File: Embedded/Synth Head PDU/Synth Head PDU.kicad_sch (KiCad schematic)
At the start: 0 parts

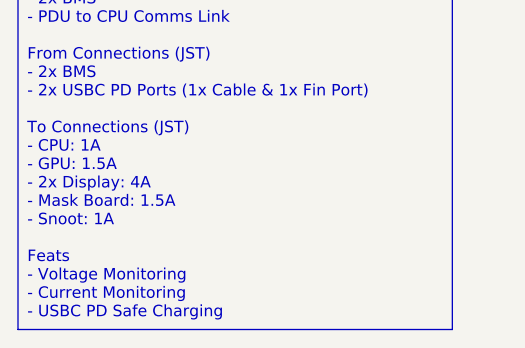
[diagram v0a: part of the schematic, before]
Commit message: KiCAD Added the schematics to drive some sensors
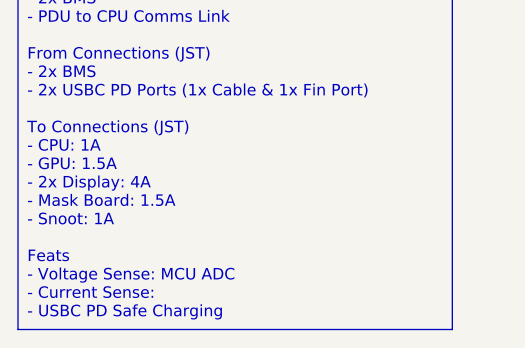
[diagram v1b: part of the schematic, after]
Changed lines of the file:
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@@
 	(generator_version "8.0")
 	(paper "A4")
-	(text_box "FFC\n- 2x BMS\n- PDU to CPU Comms Link\n\nFrom Connections (JST)\n- 2x BMS\n- 2x USBC PD Ports (1x Cable & 1x Fin Port)\n\nTo Connections (JST)\n- CPU: 1A\n- GPU: 1.5A\n- 2x Display: 4A\n- Mask Board: 1.5A\n- Snoot: 1A\n\nFeats\n- Voltage Monitoring\n- Current Monitoring\n- USBC PD Safe Charging"
+	(text_box "FFC\n- 2x BMS\n- PDU to CPU Comms Link\n\nFrom Connections (JST)\n- 2x BMS\n- 2x USBC PD Ports (1x Cable & 1x Fin Port)\n\nTo Connections (JST)\n- CPU: 1A\n- GPU: 1.5A\n- 2x Display: 4A\n- Mask Board: 1.5A\n- Snoot: 1A\n\nFeats\n- Voltage Sense: MCU ADC\n- Current Sense: \n- USBC PD Safe Charging"
 		(exclude_from_sim no)
 		(at 25.4 25.4 0)

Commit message: PDU Schematic Basically Completed
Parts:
- added D1: SL54A, Diode_SMD:D_SMA-SMB_Universal_Handsoldering, symbol Device:D
- added F1: Polyfuse, symbol Device:Polyfuse
- added J1: 10171746-00021LF, USBC_10171746_00021LF:AMPHENOL_10171746-00021LF, symbol USBC_10171746_00021LF:10171746-00021LF
- added J2, J3: JST [P], symbol Connector:Conn_01x12_Socket
- added J4: JST [USB], symbol Connector:Conn_01x06_Socket
- added J5: JST [C], symbol Connector:Conn_01x04_Socket
- added J6: JST [B], symbol Connector:Conn_01x04_Socket
- added J7: JST [G], symbol Connector:Conn_01x08_Socket
- added R1, R2: 5.1K, Resistor_SMD:R_0603_1608Metric, symbol Device:R
- added R3, R4: 4K, symbol Device:R
- added U1: FFC [K], FFC_Connector:FFC Aliexpress 0.5mm 6P, symbol FCC_Connector:FFC_6P
- added U2: TMCS1108A2BQDR, Package_SO:SOIC-8_3.9x4.9mm_P1.27mm, symbol TMCS1108:TMCS1108
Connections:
- new net: J1.A5 (CC1), R2.1
- new net: J1.B5 (CC2), R1.1
- new net: D1.1 (K), F1.1
- new net +3V3: U2.8 (VS)
- new net +5V: J5.2 (Pin_2), J5.3 (Pin_3), J6.2 (Pin_2), J6.3 (Pin_3), J7.3 (Pin_3), J7.4 (Pin_4), J7.5 (Pin_5), J7.6 (Pin_6)
- new net Analog Current: U1.5, U2.7 (Vout)
- new net Analog Voltage: R3.2, R4.1, U1.2
- new net GND: J1.A1_B12 (GND_A), J1.B1_A12 (GND_B), J1.SH1 (SHIELD), J1.SH2 (SHIELD__1), J1.SH3 (SHIELD__2), J1.SH4 (SHIELD__3), J2.1 (Pin_1), J2.10 (Pin_10), J2.11 (Pin_11), J2.12 (Pin_12), J2.2 (Pin_2), J2.3 (Pin_3), J3.1 (Pin_1), J3.10 (Pin_10), J3.11 (Pin_11), J3.12 (Pin_12), J3.2 (Pin_2), J3.3 (Pin_3), J4.1 (Pin_1), J4.6 (Pin_6), J5.1 (Pin_1), J5.4 (Pin_4), J6.1 (Pin_1), J6.4 (Pin_4), J7.1 (Pin_1), J7.2 (Pin_2), J7.7 (Pin_7), J7.8 (Pin_8), R1.2, R2.2, R4.2, U1.1, U1.6, U2.5 (GND)
- new net PWR: U2.3 (Output), U2.4 (Output)
- new net Raw PWR: F1.2, J2.4 (Pin_4), J2.5 (Pin_5), J2.6 (Pin_6), J2.7 (Pin_7), J2.8 (Pin_8), J2.9 (Pin_9), J3.4 (Pin_4), J3.5 (Pin_5), J3.6 (Pin_6), J3.7 (Pin_7), J3.8 (Pin_8), J3.9 (Pin_9), R3.1, U2.1 (Input), U2.2 (Input)
- new net USB +: J1.A6 (DP1), J1.B6 (DP2), J4.3 (Pin_3), U1.3
- new net USB -: J1.A7 (DN1), J1.B7 (DN2), J4.4 (Pin_4), U1.4
- new net USB PWR: D1.2 (A), J1.A4_B9 (VBUS_A), J1.B4_A9 (VBUS_B), J4.2 (Pin_2), J4.5 (Pin_5)
- no-connect marks 0 -> 2
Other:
- added sheet 3V3 Regulator (3V3 Reg.kicad_sch)

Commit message: PDU Nearly Complete
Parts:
- added Q1, Q2: RQ3E100BNTB, Mosfet_RQ3E100BNTB:TRANS_RQ3E100BNTB, symbol Mosfet_RQ3E100BNTB:RQ3E100BNTB
- added R5: 10K, Resistor_SMD:R_0603_1608Metric, symbol Device:R
- added R6: 1K, symbol Device:R
- added U4: RSC002P03, Mosfet_RSC002P03:RSC002P03, symbol Mosfet_RSC002P03:Mosfet_RSC002P03
- added VR1, VR2: LM1084IT-5.0_NOPB, 5V_Regulator_Fixed_LM1084IT:TO254P1054X470X1955-3, symbol 5V_Regulator_Fixed_LM1084IT:LM1084IT-5.0_NOPB
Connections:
- net +5V: now also U2.3 (Output), U2.4 (Output)
- net GND: now also R5.2, VR1.1 (ADJ/GND), VR2.1 (ADJ/GND)
- net PWR: now also F1.2, R3.1, U2.1 (Input), U2.2 (Input), VR1.2 (OUTPUT), VR2.2 (OUTPUT); no longer U2.3 (Output), U2.4 (Output)
- net USB PWR: now also R6.1, U4.2 (S)
- removed net Raw PWR: F1.2, J2.4 (Pin_4), J2.5 (Pin_5), J2.6 (Pin_6), J2.7 (Pin_7), J2.8 (Pin_8), J2.9 (Pin_9), J3.4 (Pin_4), J3.5 (Pin_5), J3.6 (Pin_6), J3.7 (Pin_7), J3.8 (Pin_8), J3.9 (Pin_9), R3.1, U2.1 (Input), U2.2 (Input)
- new net: Q1.1, VR1.3 (INPUT)
- new net: Q1.4, Q2.4, R5.1, U4.3 (D)
- new net: R6.2, U4.1 (G)
- new net: Q2.1, VR2.3 (INPUT)
- new net Raw PWR 0: J2.4 (Pin_4), J2.5 (Pin_5), J2.6 (Pin_6), J2.7 (Pin_7), J2.8 (Pin_8), J2.9 (Pin_9), Q1.5_8
- new net Raw PWR 1: J3.4 (Pin_4), J3.5 (Pin_5), J3.6 (Pin_6), J3.7 (Pin_7), J3.8 (Pin_8), J3.9 (Pin_9), Q2.5_8
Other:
- moved on the sheet: J2, J3, J4, J5, J6, J7, U1

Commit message: Prepared All Main Boards for PCB Creation
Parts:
- removed J2, J3: JST [P], symbol Connector:Conn_01x12_Socket
- added C1: 0.1uF, Capacitor_SMD:C_0603_1608Metric_Pad1.08x0.95mm_HandSolder, symbol Device:C
- added J2, J3: JST [P], Connector_PinHeader_2.54mm:PinHeader_1x08_P2.54mm_Vertical, symbol Connector:Conn_01x08_Socket
- added R10, R8: 3K, Capacitor_SMD:C_0603_1608Metric_Pad1.08x0.95mm_HandSolder, symbol Device:R
- added R11, R12: 10K, Resistor_SMD:R_0603_1608Metric_Pad0.98x0.95mm_HandSolder, symbol Device:R
- added R7, R9: 12K, Capacitor_SMD:C_0603_1608Metric_Pad1.08x0.95mm_HandSolder, symbol Device:R
- added U5: ADS1015IDGS, Package_SO:TSSOP-10_3x3mm_P0.5mm, symbol Analog_ADC:ADS1015IDGS
- F1: value Polyfuse -> BK16-500-SZ; footprint (none) -> Fuse:Fuse_Bourns_MF-RHT500
- J4: footprint (none) -> Connector_PinHeader_2.54mm:PinHeader_1x06_P2.54mm_Vertical
- J5, J6: footprint (none) -> Connector_PinHeader_2.54mm:PinHeader_1x04_P2.54mm_Vertical
- J7: footprint (none) -> Connector_PinHeader_2.54mm:PinHeader_1x08_P2.54mm_Vertical
- R3, R4, R6: footprint (none) -> Resistor_SMD:R_0603_1608Metric_Pad0.98x0.95mm_HandSolder
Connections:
- net +3V3: now also C1.1, R11.1, R12.1, U5.8 (VDD)
- net Analog Current: now also U5.5 (AIN1); no longer U1.5
- net Analog Voltage: now also U5.4 (AIN0); no longer U1.2
- net GND: now also C1.2, J2.1 (Pin_1), J2.2 (Pin_2), J2.7 (Pin_7), J2.8 (Pin_8), J3.1 (Pin_1), J3.2 (Pin_2), J3.7 (Pin_7), J3.8 (Pin_8), R10.2, R8.2, U5.1 (ADDR), U5.3 (GND)
- net Raw PWR 0: now also J2.3 (Pin_3), J2.4 (Pin_4), J2.5 (Pin_5), J2.6 (Pin_6), R7.1
- net Raw PWR 1: now also J3.3 (Pin_3), J3.4 (Pin_4), J3.5 (Pin_5), J3.6 (Pin_6), R9.1
- net at VR1.3 (INPUT): now also Q1.1_3; no longer Q1.1
- net at VR2.3 (INPUT): now also Q2.1_3; no longer Q2.1
- new net Fin Batt Voltage 0: R7.2, R8.1, U5.6 (AIN2)
- new net Fin Batt Voltage 1: R10.1, R9.2, U5.7 (AIN3)
- new net SCL: R11.2, U1.5, U5.9 (SDA)
- new net SDA: R12.2, U1.2, U5.10 (SCL)
- no-connect marks 2 -> 3
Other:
- moved on the sheet: D1, F1, J1, R1, R2, R3, R4, U2

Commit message: Prepared Circuits for Routing and Placement Tuning
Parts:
- J4: footprint Connector_PinHeader_2.54mm:PinHeader_1x06_P2.54mm_Vertical -> Connector_PinHeader_1.27mm:PinHeader_1x06_P1.27mm_Vertical
- J5, J6: footprint Connector_PinHeader_2.54mm:PinHeader_1x04_P2.54mm_Vertical -> Connector_Molex:Molex_PicoBlade_53048-0410_1x04_P1.25mm_Horizontal
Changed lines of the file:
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@@
 			)
 		)
-		(property "Footprint" "Connector_PinHeader_2.54mm:PinHeader_1x06_P2.54mm_Vertical"
+		(property "Footprint" "Connector_PinHeader_1.27mm:PinHeader_1x06_P1.27mm_Vertical"
 			(at 259.08 93.98 0)
 			(effects
@@
 			)
 		)
-		(property "Footprint" "Connector_PinHeader_2.54mm:PinHeader_1x04_P2.54mm_Vertical"
+		(property "Footprint" "Connector_Molex:Molex_PicoBlade_53048-0410_1x04_P1.25mm_Horizontal"
 			(at 259.08 128.27 0)
 			(effects
@@
 			)
 		)
-		(property "Footprint" "Connector_PinHeader_2.54mm:PinHeader_1x04_P2.54mm_Vertical"
+		(property "Footprint" "Connector_Molex:Molex_PicoBlade_53048-0410_1x04_P1.25mm_Horizontal"
 			(at 259.08 114.3 0)
 			(effects
